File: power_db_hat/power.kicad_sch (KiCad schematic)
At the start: 39 parts, among them Q1 PMOS, Q2 PMOS, U2 TPS54560BDDA, U3 TL431DBZ, U4 TL431DBZ

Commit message: update
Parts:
- added J10, J9: Conn_01x04_Pin, Connector_JST:JST_GH_SM04B-GHS-TB_1x04-1MP_P1.25mm_Horizontal, symbol Connector:Conn_01x04_Pin
- added Q3, Q4: PMOS, Package_TO_SOT_SMD:TO-252-3_TabPin2, symbol Simulation_SPICE:PMOS
- C10: renamed from C15; footprint (none) -> Capacitor_SMD:C_0805_2012Metric_Pad1.18x1.45mm_HandSolder
- C11: renamed from C10; footprint (none) -> Capacitor_SMD:C_0603_1608Metric_Pad1.08x0.95mm_HandSolder
- C12: renamed from C13; footprint (none) -> Capacitor_SMD:C_0805_2012Metric_Pad1.18x1.45mm_HandSolder
- C13: renamed from C11; footprint (none) -> Capacitor_SMD:C_0603_1608Metric_Pad1.08x0.95mm_HandSolder
- C14: renamed from C6; value 0.1uF -> 100nF; footprint (none) -> Capacitor_SMD:C_0805_2012Metric_Pad1.18x1.45mm_HandSolder
- C15: renamed from C7; footprint (none) -> Capacitor_SMD:C_0603_1608Metric_Pad1.08x0.95mm_HandSolder
- C16: renamed from C8; footprint (none) -> Capacitor_SMD:C_0603_1608Metric_Pad1.08x0.95mm_HandSolder
- C17: renamed from C9; footprint (none) -> Capacitor_SMD:C_0603_1608Metric_Pad1.08x0.95mm_HandSolder
- C18: renamed from C14; footprint (none) -> Capacitor_SMD:C_0805_2012Metric_Pad1.18x1.45mm_HandSolder
- C5: renamed from C12; footprint (none) -> Capacitor_SMD:C_0805_2012Metric_Pad1.18x1.45mm_HandSolder
- C6: renamed from C4; footprint (none) -> Capacitor_SMD:C_0603_1608Metric_Pad1.08x0.95mm_HandSolder
- C7: renamed from C3; footprint (none) -> Capacitor_SMD:C_0603_1608Metric_Pad1.08x0.95mm_HandSolder
- C8: renamed from C2; footprint (none) -> Capacitor_SMD:C_0603_1608Metric_Pad1.08x0.95mm_HandSolder
- C9: renamed from C5; footprint (none) -> Capacitor_SMD:C_0603_1608Metric_Pad1.08x0.95mm_HandSolder
- D6: renamed from D1; footprint (none) -> Diode_SMD:D_SMB-SMC_Universal_Handsoldering
- D7: renamed from D2; footprint (none) -> Diode_SMD:D_SMA-SMB_Universal_Handsoldering
- Q1: renamed from Q2; footprint (none) -> Package_TO_SOT_SMD:TO-252-3_TabPin2
- Q2: renamed from Q1; footprint (none) -> Package_TO_SOT_SMD:TO-252-3_TabPin2
- R15: renamed from R7; footprint (none) -> Resistor_SMD:R_0603_1608Metric_Pad0.98x0.95mm_HandSolder
- R16: renamed from R8; footprint (none) -> Resistor_SMD:R_0603_1608Metric_Pad0.98x0.95mm_HandSolder
- R17: renamed from R9; footprint (none) -> Resistor_SMD:R_0603_1608Metric_Pad0.98x0.95mm_HandSolder
- R18: renamed from R22; footprint (none) -> Resistor_SMD:R_0603_1608Metric_Pad0.98x0.95mm_HandSolder
- R19: renamed from R5; footprint (none) -> Resistor_SMD:R_0603_1608Metric_Pad0.98x0.95mm_HandSolder
- R20: renamed from R6; footprint (none) -> Resistor_SMD:R_0603_1608Metric_Pad0.98x0.95mm_HandSolder
- R21: renamed from R10; footprint (none) -> Resistor_SMD:R_0603_1608Metric_Pad0.98x0.95mm_HandSolder
- R22: renamed from R11; footprint (none) -> Resistor_SMD:R_0603_1608Metric_Pad0.98x0.95mm_HandSolder
- R23: renamed from R12; footprint (none) -> Resistor_SMD:R_0603_1608Metric_Pad0.98x0.95mm_HandSolder
- R24: renamed from R16; footprint (none) -> Resistor_SMD:R_0603_1608Metric_Pad0.98x0.95mm_HandSolder
- R25: renamed from R20; footprint (none) -> Resistor_SMD:R_0603_1608Metric_Pad0.98x0.95mm_HandSolder
- R26: renamed from R17; footprint (none) -> Resistor_SMD:R_0603_1608Metric_Pad0.98x0.95mm_HandSolder
- R27: renamed from R18; footprint (none) -> Resistor_SMD:R_0603_1608Metric_Pad0.98x0.95mm_HandSolder
- R28: renamed from R21; footprint (none) -> Resistor_SMD:R_0603_1608Metric_Pad0.98x0.95mm_HandSolder
- R29: renamed from R19; footprint (none) -> Resistor_SMD:R_0603_1608Metric_Pad0.98x0.95mm_HandSolder
- R30: renamed from R14; footprint (none) -> Resistor_SMD:R_0603_1608Metric_Pad0.98x0.95mm_HandSolder
- R31: renamed from R15; footprint (none) -> Resistor_SMD:R_0603_1608Metric_Pad0.98x0.95mm_HandSolder
- renumbered U3 to U2, U2 to U3
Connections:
- net GND: now also J10.3 (Pin_3), J9.3 (Pin_3)
- net VIN_12V: now also J9.1 (Pin_1), Q3.3 (S); no longer Q1.3 (S), R15.1, R17.1
- net VIN_24V: now also J10.1 (Pin_1), Q4.3 (S); no longer D7.2 (A), Q2.3 (S), R24.1, R27.1
- new net: J9.2 (Pin_2), Q3.2 (G)
- new net: J10.2 (Pin_2), Q4.2 (G)
- new net 12V_SWITCH: Q1.3 (S), Q3.1 (D), R15.1, R17.1
- new net 24V_SWITCH: D7.2 (A), Q2.3 (S), Q4.1 (D), R24.1, R27.1
- no-connect marks 0 -> 2
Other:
- note added: "Short pin 2 to pin 1 (VDD) for OFF Short pin 2 to pin 3 (GND) for ON"
- note added: "Switch"

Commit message: update
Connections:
- net 5V_OUT: no longer C15.2, C16.2, C17.2, L1.2, R30.1
- net VOUT_12V: no longer C10.1, Q1.1 (D), R21.1
- net VOUT_24V: no longer C18.1, Q2.1 (D), R29.1
- new net 12V_SNS: C10.1, Q1.1 (D), R21.1
- new net 24V_SNS: C18.1, Q2.1 (D), R29.1
- new net 5V_SNS: C15.2, C16.2, C17.2, L1.2, R30.1
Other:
- added sheet current/voltage_monitor (sensors.kicad_sch)
- note added: "TODO add reverse polarity protection"
- moved on the sheet: C12, C18, D7, Q2, R24, R25, R26, R27, R28, R29, U4

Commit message: update
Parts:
- added C19, C20: 100nF, symbol Device:C
- added D12, D13, D42: TVS_13V, Diode_SMD:D_0603_1608Metric_Pad1.05x0.95mm_HandSolder, symbol Device:D_Zener
- added D15, D16: TVS_26V, Diode_SMD:D_0603_1608Metric_Pad1.05x0.95mm_HandSolder, symbol Device:D_Zener
- added Q3: PMOS, Package_TO_SOT_SMD:TO-252-3_TabPin2, symbol Simulation_SPICE:PMOS
- added R5: 100k, symbol Device:R_US
- added R6: 10k, symbol Device:R_US
- L1: value 7.2uH -> 8.2uH; footprint (none) -> Inductors_custom:VSHB0754T_Molded_Power_Choke
- R19, R22: value 442k -> 309k
- R20: value 442k -> 53.6k
- R23: value 16.9k -> 14k
- renumbered Q3 to Q5
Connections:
- net 12V_SWITCH: now also C20.1
- net GND: now also C20.2, D12.2 (A), D13.2 (A), D15.2 (A), D16.2 (A)
- net VIN_12V: now also C19.1, D12.1 (K), D42.1 (K), Q3.1 (D), R5.1; no longer Q5.3 (S)
- net VIN_24V: now also J10.2 (Pin_2), Q4.2 (G), D15.1 (K), D16.1 (K)
- net at J9.2 (Pin_2): now also D13.1 (K), D42.2 (A), R5.2, R6.1; no longer Q5.2 (G)
- new net: C19.2, Q3.2 (G), Q5.2 (G), R6.2
- new net: Q3.3 (S), Q5.3 (S)
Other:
- note added: "not good. need to account for capacitive loads"
- moved on the sheet: J10, J9, Q4, Q5

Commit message: lol
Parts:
- removed Q4: PMOS, Package_TO_SOT_SMD:TO-252-3_TabPin2, symbol Simulation_SPICE:PMOS
- added C21, C22: 100nF, symbol Device:C
- added D43: TVS_26V, Diode_SMD:D_0603_1608Metric_Pad1.05x0.95mm_HandSolder, symbol Device:D_Zener
- added R7: 100k, symbol Device:R_US
- added R9: 10k, symbol Device:R_US
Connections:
- net 24V_SWITCH: now also Q3.1 (D), C22.1
- net GND: now also C22.2, D43.2 (A); no longer D16.2 (A)
- net VIN_12V: now also Q5.3 (S); no longer Q3.1 (D)
- net VIN_24V: now also Q3.3 (S), C21.1, R7.1; no longer J10.2 (Pin_2)
- net at C19.2, Q5.2 (G), R6.2: no longer Q3.2 (G)
- new net: D16.2 (A), D43.1 (K), J10.2 (Pin_2), R7.2, R9.1
- new net: C21.2, Q3.2 (G), R9.2
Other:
- note added: "TODO add better decoupling"
- note added: "TODO simulate"
- note removed: "not good. need to account for capacitive loads"
- moved on the sheet: C20, Q5

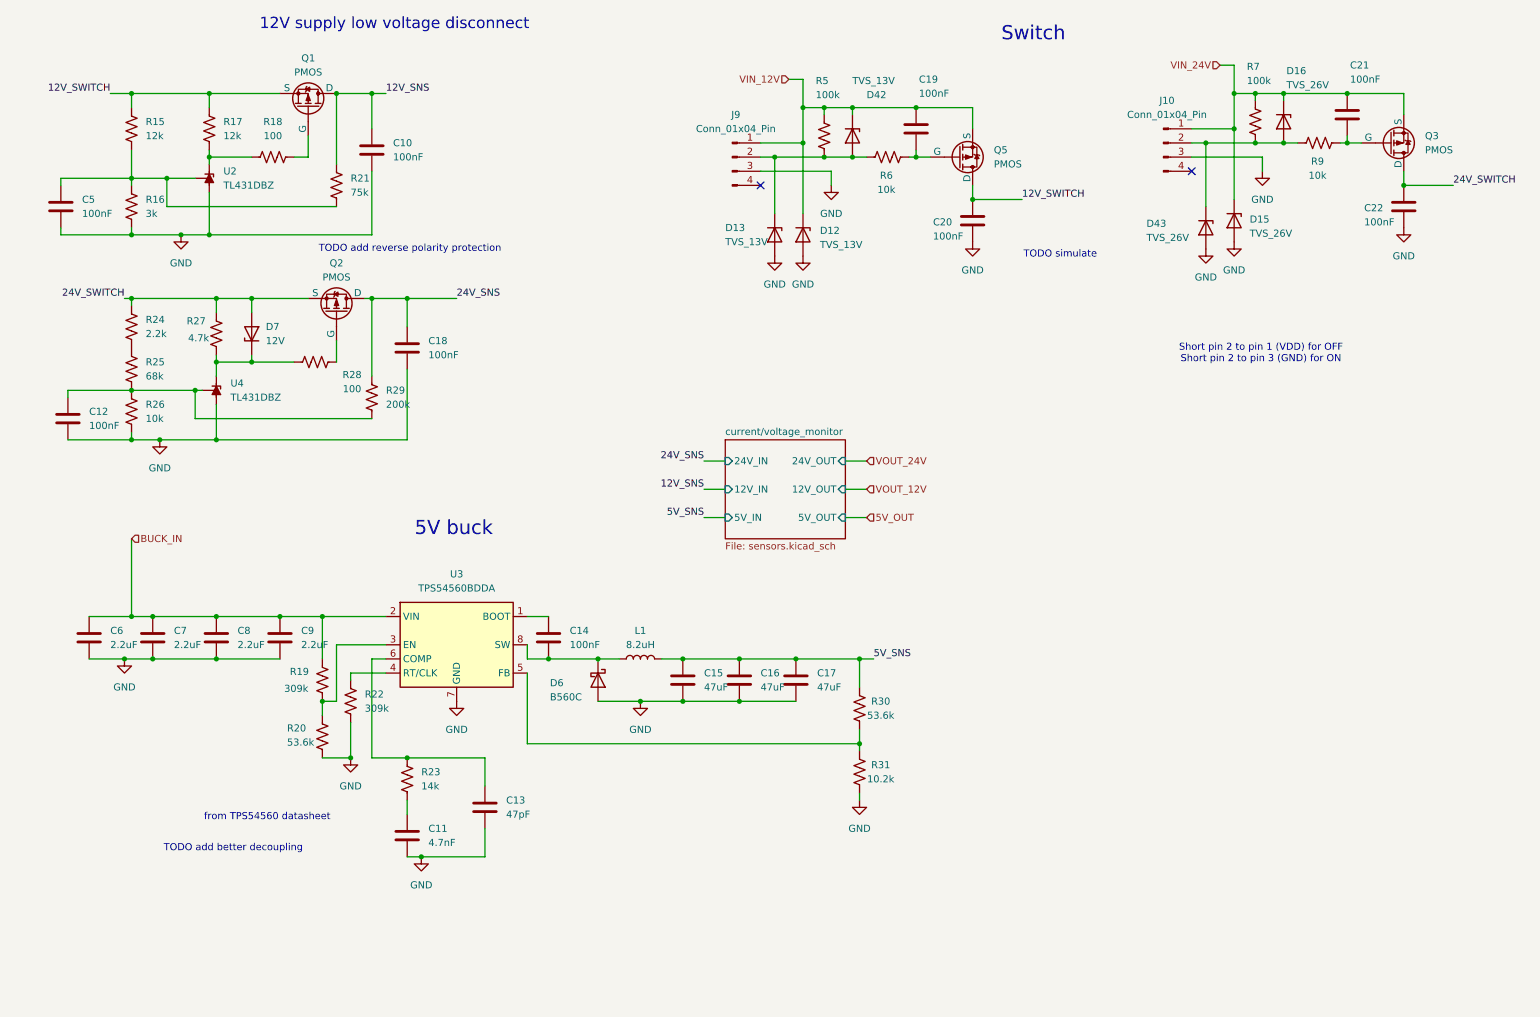
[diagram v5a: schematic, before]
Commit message: split into two PCBs
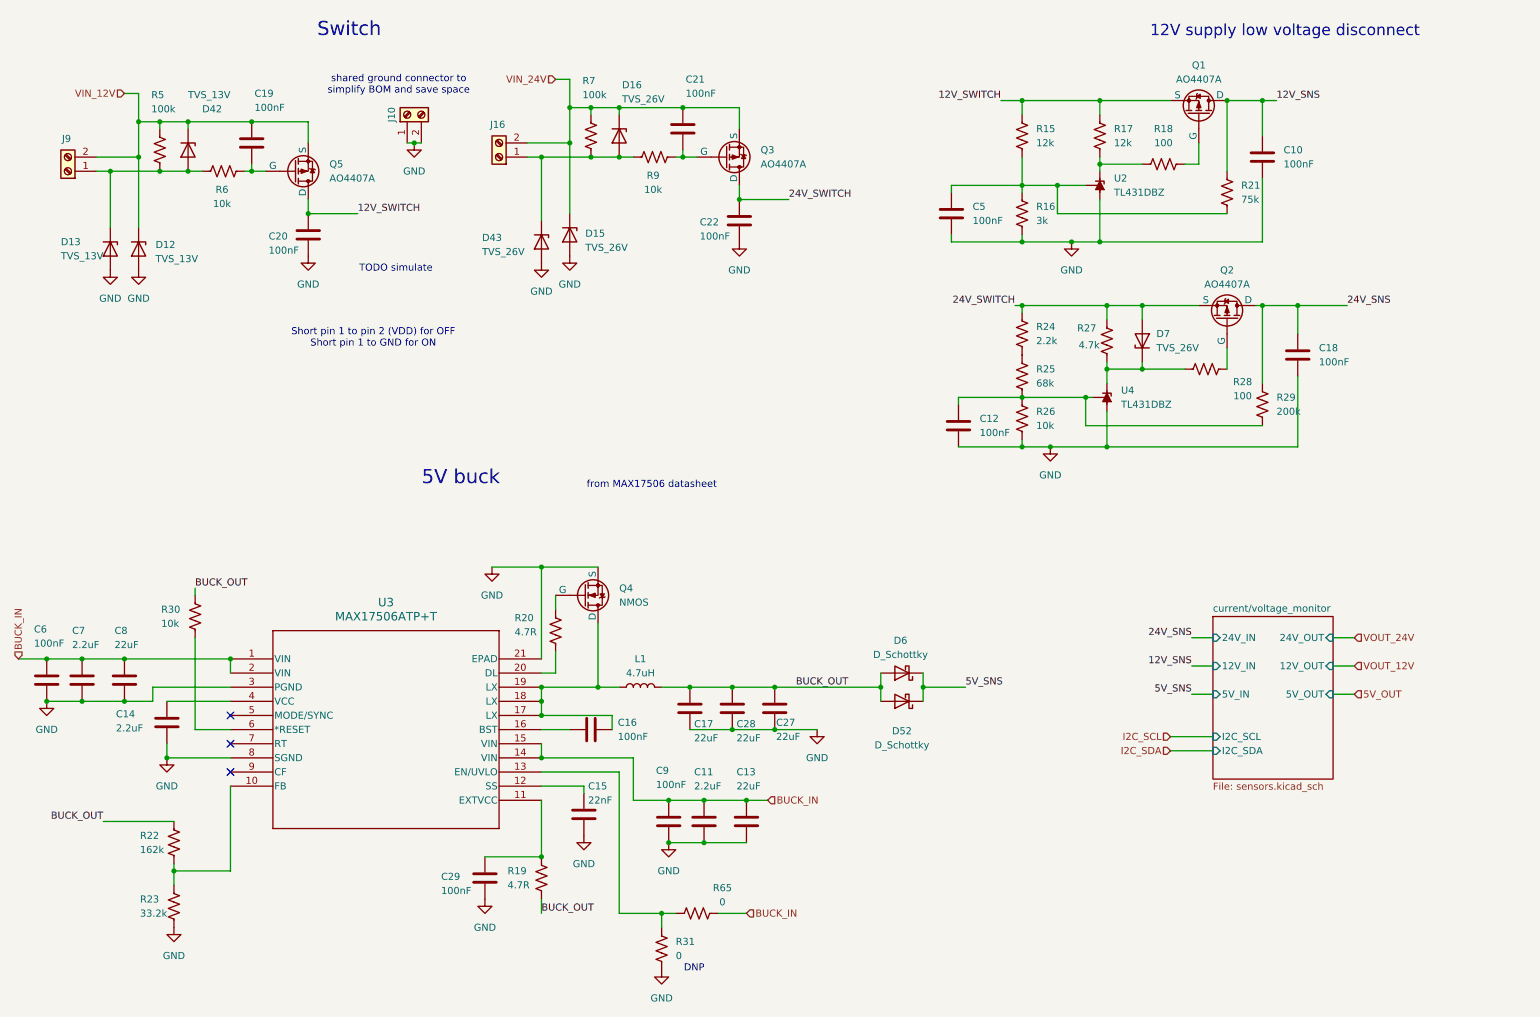
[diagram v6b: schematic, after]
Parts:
- removed J10, J9: Conn_01x04_Pin, Connector_JST:JST_GH_SM04B-GHS-TB_1x04-1MP_P1.25mm_Horizontal, symbol Connector:Conn_01x04_Pin
- removed U3: TPS54560BDDA, Package_SO:Texas_R-PDSO-G8_EP2.95x4.9mm_Mask2.4x3.1mm_ThermalVias, symbol Regulator_Switching:TPS54560BDDA
- added C27, C28: 22uF, Capacitor_SMD:C_0603_1608Metric_Pad1.08x0.95mm_HandSolder, symbol Device:C
- added C29: 100nF, Capacitor_SMD:C_0603_1608Metric_Pad1.08x0.95mm_HandSolder, symbol Device:C
- added D52: D_Schottky, Diode_SMD:D_SMA-SMB_Universal_Handsoldering, symbol Device:D_Schottky
- added J10, J16, J9: Screw_Terminal_01x02, TerminalBlock:TerminalBlock_MaiXu_MX126-5.0-02P_1x02_P5.00mm, symbol Connector:Screw_Terminal_01x02
- added Q4: NMOS, symbol Simulation_SPICE:NMOS
- added R65: 0, Resistor_SMD:R_0603_1608Metric_Pad0.98x0.95mm_HandSolder, symbol Device:R_US
- added U3: MAX17506ATP+T, MAX17506:21-0140L_T2055-4_MXM, symbol MAX17506:MAX17506ATP+T
- C10, C12, C18, C5: footprint Capacitor_SMD:C_0805_2012Metric_Pad1.18x1.45mm_HandSolder -> Capacitor_SMD:C_0603_1608Metric_Pad1.08x0.95mm_HandSolder
- C11: value 4.7nF -> 2.2uF
- C13: value 47pF -> 22uF
- C14: value 100nF -> 2.2uF; footprint Capacitor_SMD:C_0805_2012Metric_Pad1.18x1.45mm_HandSolder -> Capacitor_SMD:C_0603_1608Metric_Pad1.08x0.95mm_HandSolder
- C15: value 47uF -> 22nF
- C16: value 47uF -> 100nF
- C17: value 47uF -> 22uF
- C19, C20, C21, C22: footprint (none) -> Capacitor_SMD:C_0603_1608Metric_Pad1.08x0.95mm_HandSolder
- C6, C9: value 2.2uF -> 100nF
- C8: value 2.2uF -> 22uF
- D6: value B560C -> D_Schottky; footprint Diode_SMD:D_SMB-SMC_Universal_Handsoldering -> Diode_SMD:D_SMA-SMB_Universal_Handsoldering
- D7: value 12V -> TVS_26V
- L1: value 8.2uH -> 4.7uH; footprint Inductors_custom:VSHB0754T_Molded_Power_Choke -> Inductor_TDK:IND_B82477G4472M000
- Q1, Q2, Q3, Q5: value PMOS -> AO4407A; footprint Package_TO_SOT_SMD:TO-252-3_TabPin2 -> (none)
- R19: value 309k -> 4.7R
- R20: value 53.6k -> 4.7R
- R22: value 309k -> 162k
- R23: value 14k -> 33.2k
- R30: value 53.6k -> 10k
- R31: value 10.2k -> 0
- R5, R6, R7, R9: footprint (none) -> Resistor_SMD:R_0603_1608Metric_Pad0.98x0.95mm_HandSolder
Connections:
- net 5V_SNS: now also D6.1 (K), D52.1 (K); no longer C15.2, C16.2, C17.2, L1.2, R30.1
- net BUCK_IN: now also C11.1, C13.1, R65.1, U3.1 (VIN), U3.14 (VIN), U3.15 (VIN), U3.2 (VIN); no longer R19.1
- net GND: now also C11.2, C13.2, C14.2, C15.2, C17.2, R23.2, C27.2, C28.2, C29.2, J10.1 (Pin_1), J10.2 (Pin_2), Q4.3 (S), U3.21 (EPAD), U3.3 (PGND), U3.8 (SGND); no longer C11.1, C13.1, C15.1, C16.1, C17.1, D6.2 (A), R20.2, R22.2
- net VIN_12V: now also J9.2 (Pin_2)
- net VIN_24V: now also J16.2 (Pin_2)
- net at D16.2 (A), D43.1 (K), R7.2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: now also J16.1 (Pin_1)
- net at D13.1 (K), D42.2 (A), R5.2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: now also J9.1 (Pin_1)
- net at R30.2: now also U3.6 (*RESET); no longer R31.1
- net at R20.1: now also Q4.2 (G); no longer R19.2
- net at C14.1: now also U3.4 (VCC)
- net BUCK_OUT: now reaches R22.1
- net BUCK_OUT: now also C17.1, D6.2 (A), L1.2, R19.2, R30.1, C27.1, C28.1, D52.2 (A)
- net at R23.1: now also R22.2, U3.10 (FB); no longer C13.2
- new net: C15.1, U3.12 (SS)
- new net: C29.1, R19.1, U3.11 (EXTVCC)
- new net: R31.1, R65.2, U3.13 (EN/UVLO)
- new net: C16.1, U3.16 (BST)
- new net: C16.2, L1.1, Q4.1 (D), U3.17 (LX), U3.18 (LX), U3.19 (LX)
- new net: R20.2, U3.20 (DL)
- no-connect marks 2 -> 3
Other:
- sheet current/voltage_monitor ports: added I2C_SCL, I2C_SDA; removed none
- note added: "DNP"
- note added: "Short pin 1 to pin 2 (VDD) for OFF Short pin 1 to GND for ON"
- note added: "from MAX17506 datasheet"
- note added: "shared ground connector to simplify BOM and save space"
- note removed: "Short pin 2 to pin 1 (VDD) for OFF Short pin 2 to pin 3 (GND) for ON"
- note removed: "TODO add better decoupling"
- note removed: "TODO add reverse polarity protection"
- note removed: "from TPS54560 datasheet"
- moved on the sheet: C10, C12, C18, C19, C20, C21, C22, C5, D12, D13, D15, D16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

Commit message: lol
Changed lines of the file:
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@@
 	(text "from MAX17506 datasheet\n"
 		(exclude_from_sim no)
-		(at 129.032 103.378 0)
+		(at 87.122 110.236 0)
 		(effects
 			(font
@@
 	(text "5V buck\n"
 		(exclude_from_sim no)
-		(at 94.742 102.108 0)
+		(at 86.868 105.156 0)
 		(effects
 			(font

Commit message: UPDATE
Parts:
- removed C10, C16, C19, C20, C29, C5, C6, C9: 100nF, Capacitor_SMD:C_0603_1608Metric_Pad1.08x0.95mm_HandSolder, symbol Device:C
- removed C11, C14, C7: 2.2uF, Capacitor_SMD:C_0603_1608Metric_Pad1.08x0.95mm_HandSolder, symbol Device:C
- removed C13, C17, C27, C28, C8: 22uF, Capacitor_SMD:C_0603_1608Metric_Pad1.08x0.95mm_HandSolder, symbol Device:C
- removed C15: 22nF, Capacitor_SMD:C_0603_1608Metric_Pad1.08x0.95mm_HandSolder, symbol Device:C
- removed D12, D13, D42: TVS_13V, Diode_SMD:D_0603_1608Metric_Pad1.05x0.95mm_HandSolder, symbol Device:D_Zener
- removed J9: Screw_Terminal_01x02, TerminalBlock:TerminalBlock_MaiXu_MX126-5.0-02P_1x02_P5.00mm, symbol Connector:Screw_Terminal_01x02
- removed L1: 4.7uH, Inductor_TDK:IND_B82477G4472M000, symbol Device:L
- removed Q1, Q5: AO4407A, symbol Simulation_SPICE:PMOS
- removed Q4: NMOS, symbol Simulation_SPICE:NMOS
- removed R15, R17: 12k, Resistor_SMD:R_0603_1608Metric_Pad0.98x0.95mm_HandSolder, symbol Device:R_US
- removed R16: 3k, Resistor_SMD:R_0603_1608Metric_Pad0.98x0.95mm_HandSolder, symbol Device:R_US
- removed R18: 100, Resistor_SMD:R_0603_1608Metric_Pad0.98x0.95mm_HandSolder, symbol Device:R_US
- removed R19, R20: 4.7R, Resistor_SMD:R_0603_1608Metric_Pad0.98x0.95mm_HandSolder, symbol Device:R_US
- removed R21: 75k, Resistor_SMD:R_0603_1608Metric_Pad0.98x0.95mm_HandSolder, symbol Device:R_US
- removed R22: 162k, Resistor_SMD:R_0603_1608Metric_Pad0.98x0.95mm_HandSolder, symbol Device:R_US
- removed R23: 33.2k, Resistor_SMD:R_0603_1608Metric_Pad0.98x0.95mm_HandSolder, symbol Device:R_US
- removed R30, R6: 10k, Resistor_SMD:R_0603_1608Metric_Pad0.98x0.95mm_HandSolder, symbol Device:R_US
- removed R31, R65: 0, Resistor_SMD:R_0603_1608Metric_Pad0.98x0.95mm_HandSolder, symbol Device:R_US
- removed R5: 100k, Resistor_SMD:R_0603_1608Metric_Pad0.98x0.95mm_HandSolder, symbol Device:R_US
- removed U2: TL431DBZ, Package_TO_SOT_SMD:SOT-23, symbol Reference_Voltage:TL431DBZ
- removed U3: MAX17506ATP+T, MAX17506:21-0140L_T2055-4_MXM, symbol MAX17506:MAX17506ATP+T
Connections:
- net BUCK_OUT renamed bucks/BUCK_OUT_5V
- no-connect marks 3 -> 0
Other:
- added sheet bucks (bucks.kicad_sch)
- note added: "extra ground connector to simplify BOM and save space"
- note removed: "5V buck"
- note removed: "DNP"
- note removed: "from MAX17506 datasheet"
- note removed: "shared ground connector to simplify BOM and save space"
- moved on the sheet: C12, C18, C21, C22, D15, D16, D43, D7, J10, J16, Q2, Q3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
